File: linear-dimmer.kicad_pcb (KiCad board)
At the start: 2 copper layers, 49.3 x 30.4 mm, 31 parts, among them CON1 BARREL_JACK, P1 POWER, Q1 BUK6207-55C, SW1 Switch_SPDT_x2, U1 LM78L05ACZ, U2 MCP6072, U3 REF3012, U4 MCP65R41T

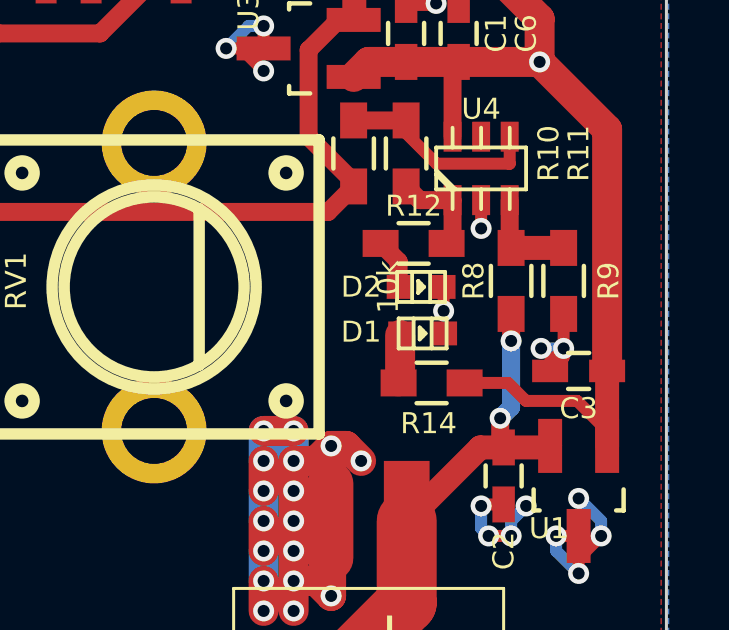
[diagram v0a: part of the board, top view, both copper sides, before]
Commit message: Put the power on led to comparator so that blue changes to red on battery low
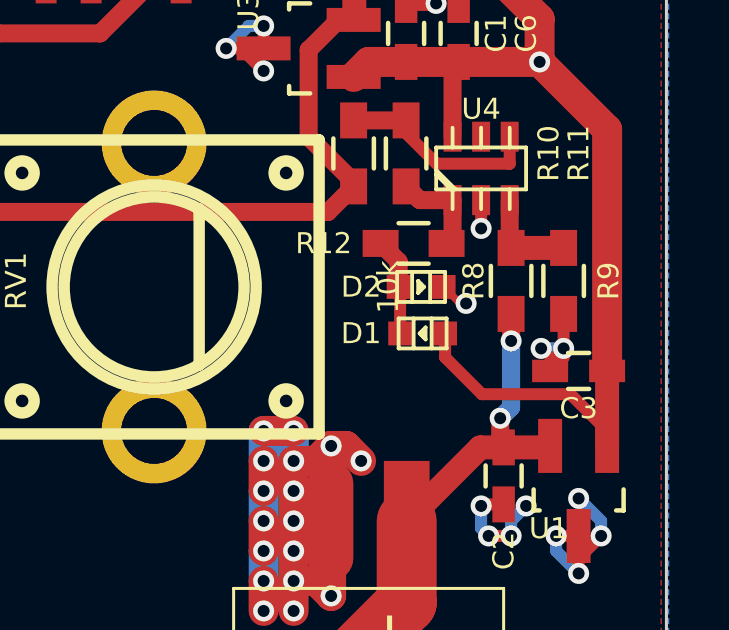
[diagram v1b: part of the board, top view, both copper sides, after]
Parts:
- removed R14: 220, Resistors_SMD:R_0603_HandSoldering
- R4: value 3.74k -> 45.3k
- R6, R7: value 1R -> 0R5
- turned D1 to 180 degrees
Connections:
- D1 pad 1: Net-(D1-Pad1) -> +5V
- D1 pad 2: GND -> Net-(D1-Pad2)
- D2 pad 1: Net-(D2-Pad1) -> Net-(D1-Pad2)
- R12 pad 2: Net-(D2-Pad1) -> Net-(D1-Pad2)
- SW1 pad : GND -> (no net)
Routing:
- net Net-(D1-Pad2): track 0.00 -> 3.27 mm
- net (no net): track 0.00 -> 3.02 mm, vias 0 -> 3
- net GND: track 133.0 -> 130.2 mm, vias 92 -> 89
- net +5V: track 64.1 -> 65.9 mm
- net Net-(D2-Pad1): track 1.70 -> 0.00 mm
- net Net-(D1-Pad1): track 1.57 -> 0.00 mm

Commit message: Implement changes in PCB
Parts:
- added R13: 2k, Resistors_SMD:R_0603_HandSoldering, F.Cu at (130.5, 94.5)
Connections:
- RV1 pad 1: +1.2V -> GND
- RV1 pad 3: GND -> +1.2V
- SW1 pad : (no net) -> GND
- U4 pad 3: Net-(R8-Pad2) -> Net-(R10-Pad2)
- U4 pad 4: Net-(R10-Pad2) -> Net-(R8-Pad2)
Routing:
- net /OUTPUT: track 71.3 -> 83.5 mm
- net GND: track 130.2 -> 137.3 mm, vias 89 -> 93
- net (no net): track 3.02 -> 0.00 mm, vias 3 -> 0
- net VCC: track 37.8 -> 40.7 mm
- net Net-(R8-Pad2): track 3.36 -> 5.88 mm
- net +1.2V: track 22.6 -> 24.8 mm
